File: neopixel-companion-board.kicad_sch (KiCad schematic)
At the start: 18 parts, among them J1 VIN, J11 Conn_01x03, J6 Conn_01x04, U3 74LVC1G17

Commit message: initial beta stuff
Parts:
- J11: footprint KlipperExpander:PinHeader_1x03_P2.54mm_Vertical -> Connector_Molex:Molex_Micro-Fit_3.0_43650-0315_1x03_P3.00mm_Vertical
- J5: renamed from J1; footprint (none) -> Connector_Phoenix_MSTB:PhoenixContact_MSTBA_2,5_2-G_1x02_P5.00mm_Horizontal
- renumbered R3 to R2, R2 to R3
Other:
- moved on the sheet: C1, C2, C3, C4, J11, J5, J6, R2, R4, U3

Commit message: Changed connector and added library files
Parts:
- J5: footprint Connector_Phoenix_MSTB:PhoenixContact_MSTBA_2,5_2-G_1x02_P5.00mm_Horizontal -> Neopixel-Companion:796949-2
- U3: footprint KlipperExpander:SOT-753 -> Neopixel-Companion:SOT-753
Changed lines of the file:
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@@
       (effects (font (size 1.27 1.27)))
     )
-    (property "Footprint" "KlipperExpander:SOT-753" (at 68.58 106.68 0)
+    (property "Footprint" "Neopixel-Companion:SOT-753" (at 68.58 106.68 0)
       (effects (font (size 1.27 1.27)) hide)
     )
@@
       (effects (font (size 1.27 1.27)))
     )
-    (property "Footprint" "KlipperExpander:SOT-753" (at 68.58 78.74 0)
+    (property "Footprint" "Neopixel-Companion:SOT-753" (at 68.58 78.74 0)
       (effects (font (size 1.27 1.27)) hide)
     )
@@
       (effects (font (size 1.27 1.27)))
     )
-    (property "Footprint" "KlipperExpander:SOT-753" (at 148.59 106.68 0)
+    (property "Footprint" "Neopixel-Companion:SOT-753" (at 148.59 106.68 0)
       (effects (font (size 1.27 1.27)) hide)
     )
@@
       (effects (font (size 1.27 1.27)))
     )
-    (property "Footprint" "KlipperExpander:SOT-753" (at 148.59 78.74 0)
+    (property "Footprint" "Neopixel-Companion:SOT-753" (at 148.59 78.74 0)
       (effects (font (size 1.27 1.27)) hide)
     )
@@
       (effects (font (size 1.27 1.27)))
     )
-    (property "Footprint" "Connector_Phoenix_MSTB:PhoenixContact_MSTBA_2,5_2-G_1x02_P5.00mm_Horizontal" (at 38.1 62.23 0)
-      (effects (font (size 1.27 1.27)) hide)
-    )
+    (property "Footprint" "Neopixel-Companion:796949-2" (at 38.1 62.23 0)
+      (effects (font (size 1.27 1.27)) hide)
+    )

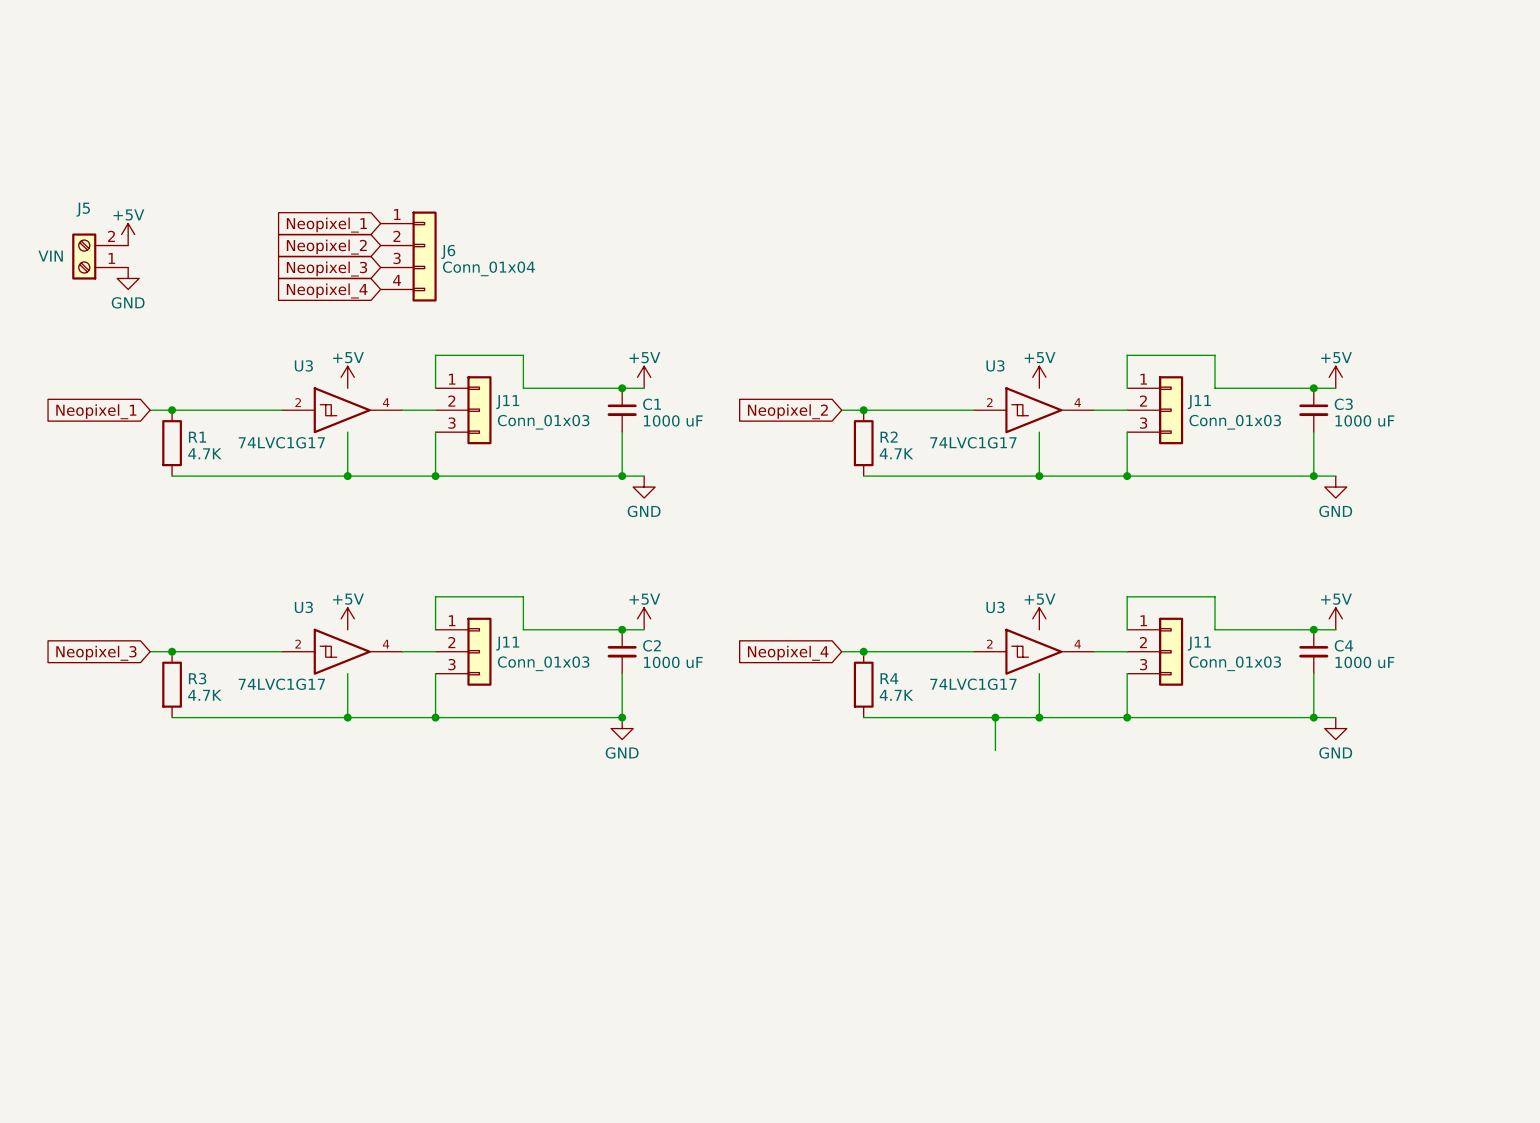
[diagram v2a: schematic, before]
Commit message: Replaced single schmitt triggers with a 4 bit level shifter
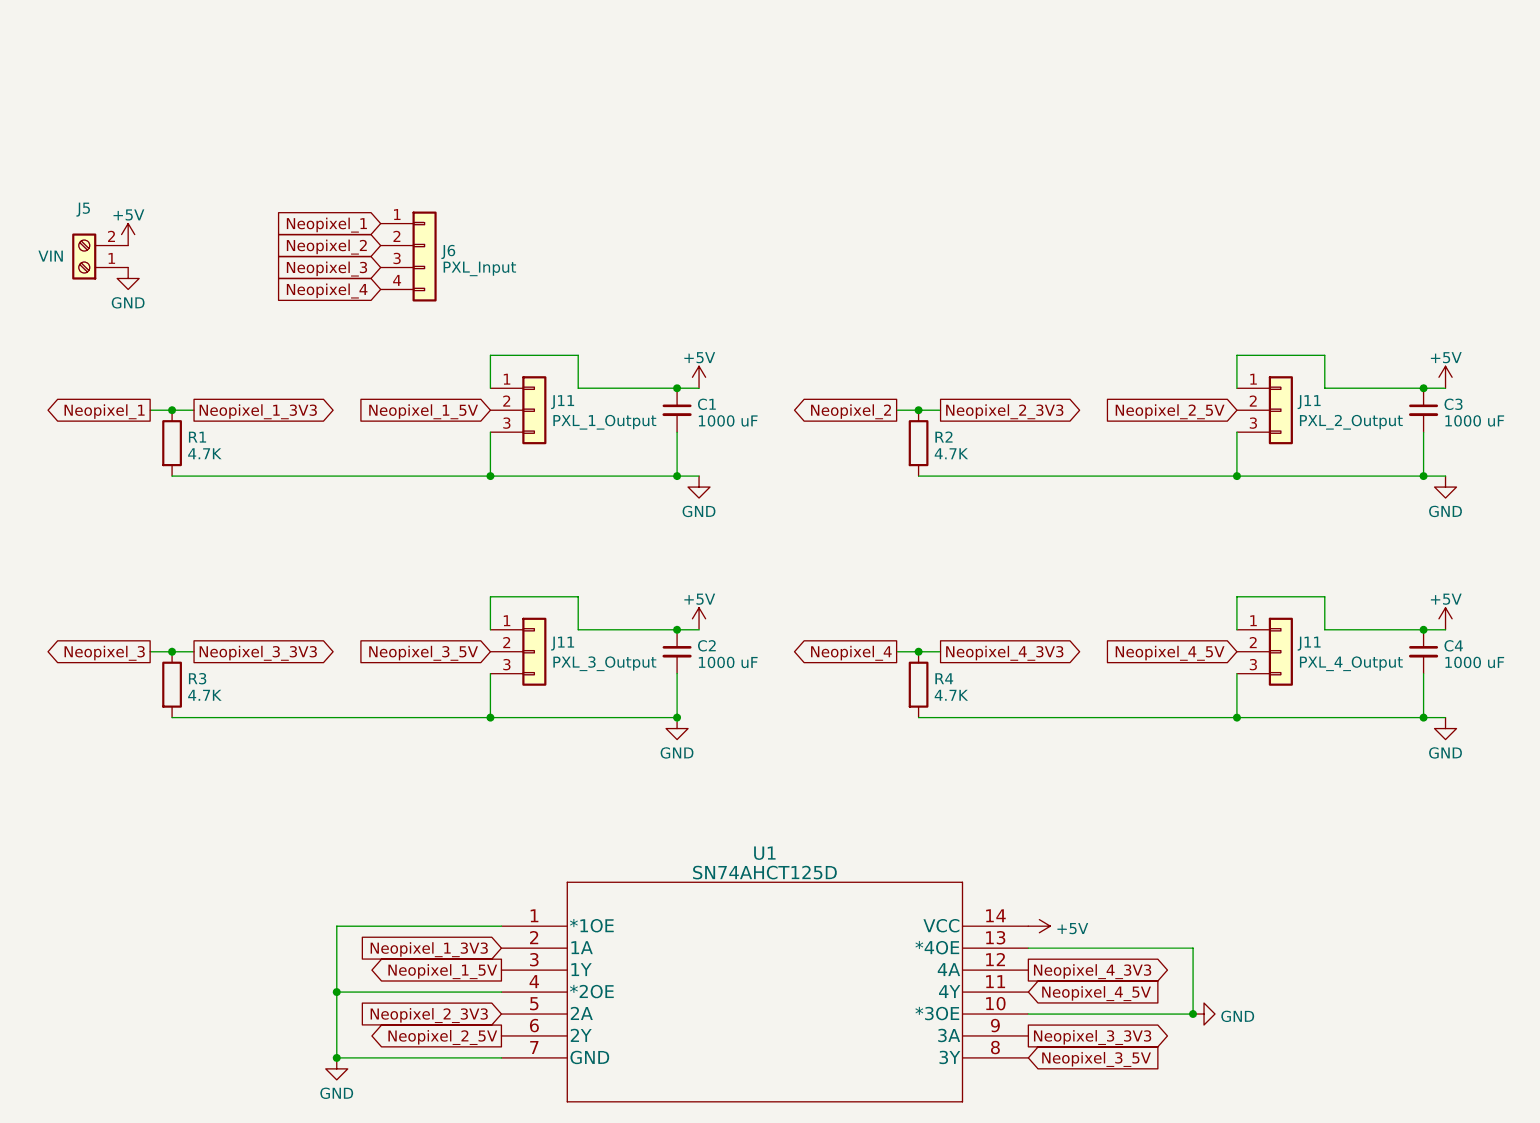
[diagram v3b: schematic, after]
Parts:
- removed U3 (x4): 74LVC1G17, Neopixel-Companion:SOT-753, symbol KlipperExpander:74LVC1G17
- added U1: SN74AHCT125D, Neopixel-Companion:SN74AHCT125D, symbol Ti-Extra:SN74AHCT125D
- J11: value Conn_01x03 -> PXL_2_Output
- J11: value Conn_01x03 -> PXL_1_Output
- J11: value Conn_01x03 -> PXL_4_Output
- J11: value Conn_01x03 -> PXL_3_Output
- J6: value Conn_01x04 -> PXL_Input
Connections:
- net +5V: now also U1.14 (VCC)
- net GND: now also U1.1 (*1OE), U1.10 (*3OE), U1.13 (*4OE), U1.4 (*2OE), U1.7 (GND)
- net Neopixel_1: now also U1.2 (1A)
- net Neopixel_2: now also U1.5 (2A)
- net Neopixel_3: now also U1.9 (3A)
- net Neopixel_4: now also U1.12 (4A)
- net Neopixel_3_5V: now reaches J11.2 (Pin_2)
- net Neopixel_3_5V: now also U1.8 (3Y)
- net Neopixel_1_5V: now reaches J11.2 (Pin_2)
- net Neopixel_1_5V: now also U1.3 (1Y)
- net Neopixel_4_5V: now reaches J11.2 (Pin_2)
- net Neopixel_4_5V: now also U1.11 (4Y)
- net Neopixel_2_5V: now reaches J11.2 (Pin_2)
- net Neopixel_2_5V: now also U1.6 (2Y)
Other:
- moved on the sheet: C1, C2, C3, C4, J11, R2, R4

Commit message: Added LCSC parts and gerbers
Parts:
- C1, C2, C3, C4: LCSC (none) -> C106511
- J11: symbol KlipperExpander:Conn_01x03 -> Connector_Generic:Conn_01x03; LCSC (none) -> C293546
- J5: LCSC (none) -> C430601
- J6: LCSC (none) -> C144395
- R1, R2, R3, R4: LCSC (none) -> C104821
- U1: LCSC (none) -> C155176
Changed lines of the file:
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@@
+      (effects (font (size 1.27 1.27)) hide)
+    )
+    (property "LCSC" "C104821" (at 48.26 82.55 0)
       (effects (font (size 1.27 1.27)) hide)
     )
@@
     )
     (property "Datasheet" "~" (at 77.47 59.69 0)
+      (effects (font (size 1.27 1.27)) hide)
+    )
+    (property "LCSC" "C144395" (at 77.47 59.69 0)
       (effects (font (size 1.27 1.27)) hide)
     )
@@
     )
   )
-  (symbol (lib_id "KlipperExpander:Conn_01x03") (at 176.53 78.74 0) (unit 1)
+  (symbol (lib_id "Connector_Generic:Conn_01x03") (at 176.53 78.74 0) (unit 1)
     (in_bom yes) (on_board yes) (dnp no)
     (property "Reference" "J11" (at 178.562 77.6732 0)
@@
     )
     (property "Datasheet" "~" (at 176.53 78.74 0)
+      (effects (font (size 1.27 1.27)) hide)
+    )
+    (property "LCSC" "C293546" (at 176.53 78.74 0)
       (effects (font (size 1.27 1.27)) hide)
     )
@@
     )
   )
-  (symbol (lib_id "KlipperExpander:Conn_01x03") (at 90.17 78.74 0) (unit 1)
+  (symbol (lib_id "Connector_Generic:Conn_01x03") (at 90.17 78.74 0) (unit 1)
     (in_bom yes) (on_board yes) (dnp no)
     (property "Reference" "J11" (at 92.202 77.6732 0)
@@
     )
     (property "Datasheet" "~" (at 90.17 78.74 0)
+      (effects (font (size 1.27 1.27)) hide)
+    )
+    (property "LCSC" "C293546" (at 90.17 78.74 0)
       (effects (font (size 1.27 1.27)) hide)
     )
@@
       (effects (font (size 1.27 1.27)) hide)
     )
+    (property "LCSC" "C106511" (at 193.04 106.68 0)
+      (effects (font (size 1.27 1.27)) hide)
+    )
     (pin "1")
     (pin "2")
@@
       (effects (font (size 1.27 1.27)) hide)
     )
+    (property "LCSC" "C104821" (at 134.62 110.49 0)
+      (effects (font (size 1.27 1.27)) hide)
+    )
     (pin "1")
     (pin "2")
@@
       (effects (font (size 1.27 1.27)) hide)
     )
+    (property "LCSC" "C106511" (at 106.68 106.68 0)
+      (effects (font (size 1.27 1.27)) hide)
+    )
     (pin "1")
     (pin "2")
@@
     )
     (property "Datasheet" "~" (at 134.62 82.55 0)
+      (effects (font (size 1.27 1.27)) hide)
+    )
+    (property "LCSC" "C104821" (at 134.62 82.55 0)
       (effects (font (size 1.27 1.27)) hide)
     )
@@
       (effects (font (size 1.27 1.27)) hide)
     )
+    (property "LCSC" "C106511" (at 106.68 78.74 0)
+      (effects (font (size 1.27 1.27)) hide)
+    )
     (pin "1")
     (pin "2")
@@
       (effects (font (size 1.27 1.27)) hide)
     )
+    (property "LCSC" "C106511" (at 193.04 78.74 0)
+      (effects (font (size 1.27 1.27)) hide)
+    )
     (pin "1")
     (pin "2")
@@
     )
   )
-  (symbol (lib_id "KlipperExpander:Conn_01x03") (at 176.53 106.68 0) (unit 1)
+  (symbol (lib_id "Connector_Generic:Conn_01x03") (at 176.53 106.68 0) (unit 1)
     (in_bom yes) (on_board yes) (dnp no)
     (property "Reference" "J11" (at 178.562 105.6132 0)
@@
     )
     (property "Datasheet" "~" (at 176.53 106.68 0)
+      (effects (font (size 1.27 1.27)) hide)
+    )
+    (property "LCSC" "C293546" (at 176.53 106.68 0)
       (effects (font (size 1.27 1.27)) hide)
     )
@@
     (property "Datasheet" "" (at 86.36 138.43 0)
       (effects (font (size 1.524 1.524)))
+    )
+    (property "LCSC" "C155176" (at 86.36 138.43 0)
+      (effects (font (size 1.27 1.27)) hide)
     )
     (pin "1")
@@
       (effects (font (size 1.27 1.27)) hide)
     )
+    (property "LCSC" "C430601" (at 38.1 62.23 0)
+      (effects (font (size 1.27 1.27)) hide)
+    )
     (pin "1")
     (pin "2")
@@
     )
   )
-  (symbol (lib_id "KlipperExpander:Conn_01x03") (at 90.17 106.68 0) (unit 1)
+  (symbol (lib_id "Connector_Generic:Conn_01x03") (at 90.17 106.68 0) (unit 1)
     (in_bom yes) (on_board yes) (dnp no)
     (property "Reference" "J11" (at 92.202 105.6132 0)
@@
     )
     (property "Datasheet" "~" (at 90.17 106.68 0)
+      (effects (font (size 1.27 1.27)) hide)
+    )
+    (property "LCSC" "C293546" (at 90.17 106.68 0)
       (effects (font (size 1.27 1.27)) hide)
     )
@@
       (effects (font (size 1.27 1.27)) hide)
     )
+    (property "LCSC" "C104821" (at 48.26 110.49 0)
+      (effects (font (size 1.27 1.27)) hide)
+    )
